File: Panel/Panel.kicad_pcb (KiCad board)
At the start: 2 copper layers, 100 x 100 mm, 83 parts, among them J1 Conn_01x03, J10 Conn_01x02, J11 Conn_01x03, J12 Conn_01x03, J2 USB_C_Receptacle_USB2.0, J3 Conn_01x02, J4 Conn_02x06_Odd_Even, J5 Conn_01x07, J6 Conn_01x02, J7 Conn_01x02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

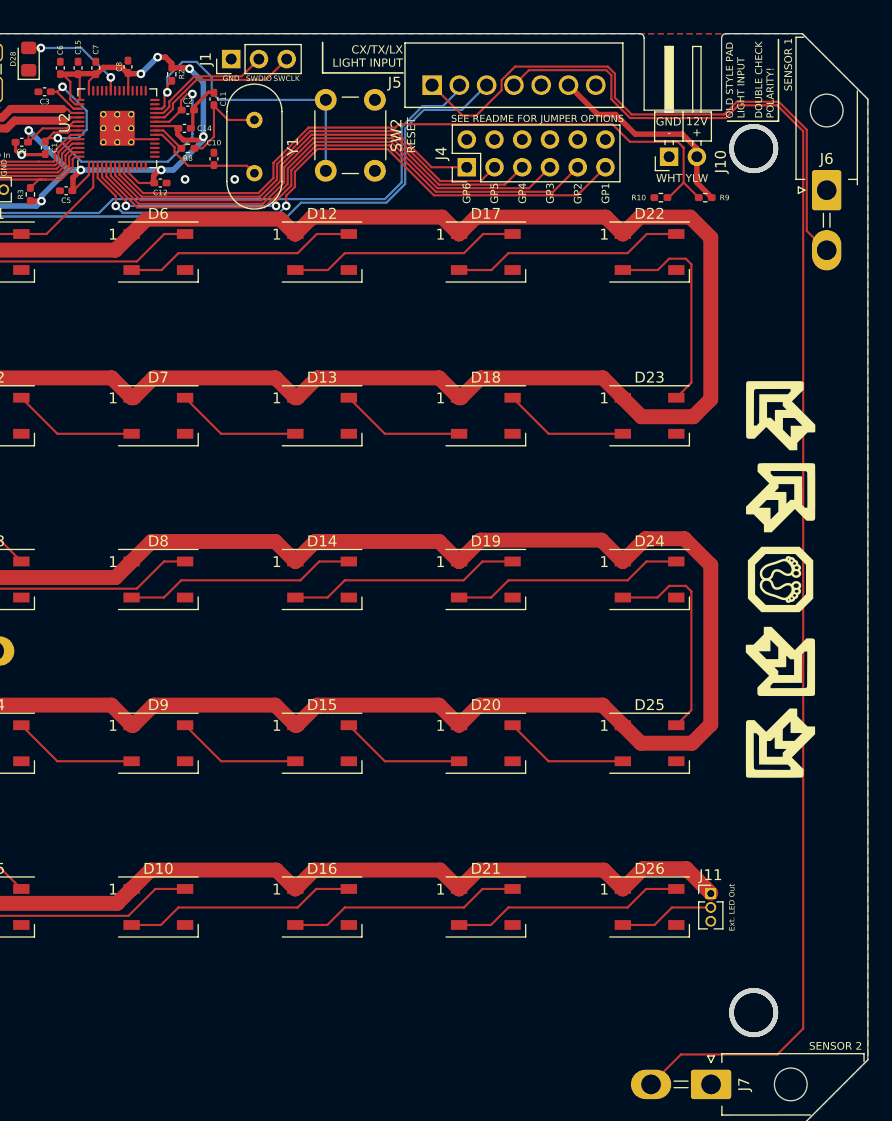
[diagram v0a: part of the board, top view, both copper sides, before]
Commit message: Add RS485 functionality & addons, several fixes
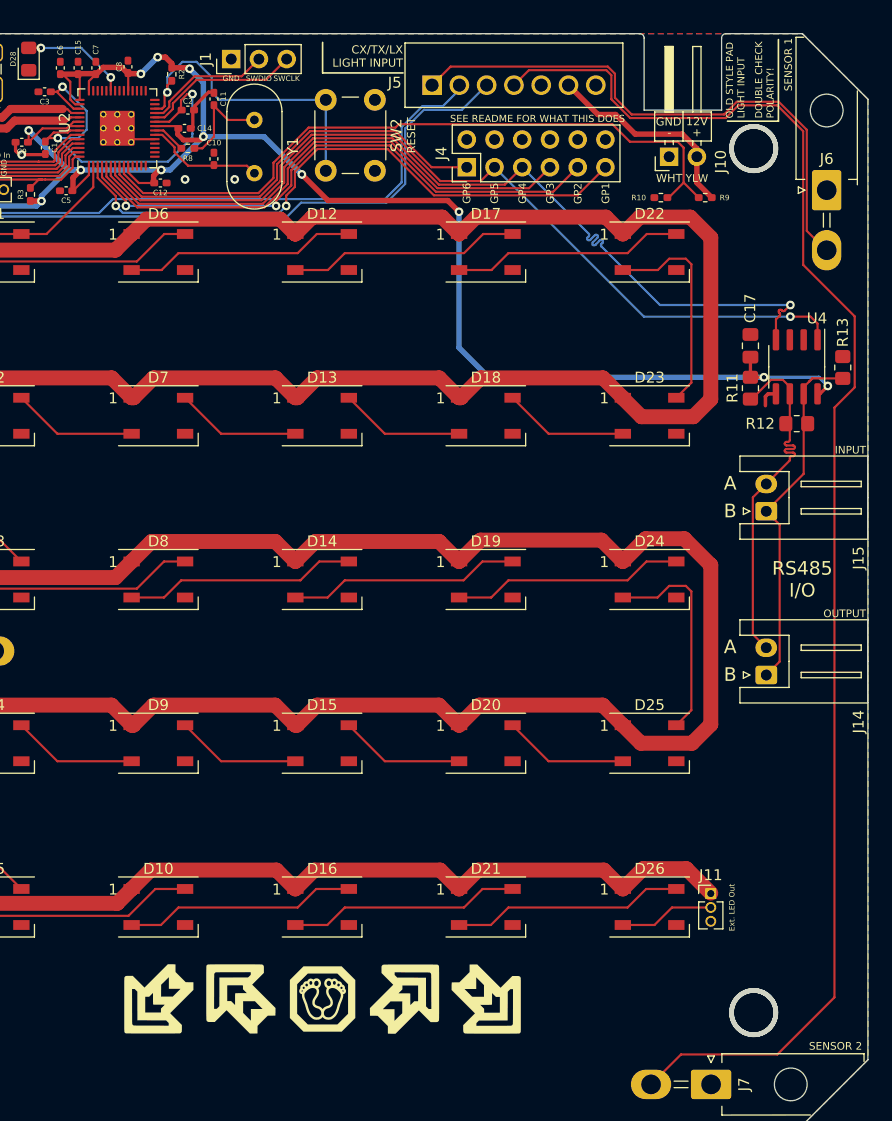
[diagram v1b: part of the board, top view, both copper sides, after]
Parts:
- added C17: 100nF, Capacitor_SMD:C_0805_2012Metric_Pad1.18x1.45mm_HandSolder, F.Cu at (169.2, 78.6)
- added J14: Conn_01x02, Connector_JST:JST_XH_S2B-XH-A_1x02_P2.50mm_Horizontal, F.Cu at (170.7, 108.8)
- added J15: Conn_01x02, Connector_JST:JST_XH_S2B-XH-A_1x02_P2.50mm_Horizontal, F.Cu at (170.7, 93.8)
- added R11: 4.7k, Resistor_SMD:R_0805_2012Metric_Pad1.20x1.40mm_HandSolder, F.Cu at (169.2, 82.5)
- added R12: 120, Resistor_SMD:R_0805_2012Metric_Pad1.20x1.40mm_HandSolder, F.Cu at (173.5, 85.7)
- added R13: 4.7k, Resistor_SMD:R_0805_2012Metric_Pad1.20x1.40mm_HandSolder, F.Cu at (177.7, 80.6)
- added U4: SP3485EN, Package_SO:SOIC-8_3.9x4.9mm_P1.27mm, F.Cu at (173.5, 80.5)
- moved G*** 78.1 mm to (115.0, 138.4), turned to 180 degrees
- moved G*** 67.5 mm to (122.5, 138.4), turned to 90 degrees
- moved G*** 56.9 mm to (130.0, 138.4), turned to 0 degrees
- moved G*** 46.3 mm to (137.5, 138.4), turned to 0 degrees
- moved G*** 35.7 mm to (145.0, 138.4), turned to -90 degrees
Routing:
- net +3V3: track 117.1 -> 195.2 mm, vias 10 -> 14
- net GPIO5: track 42.2 -> 79.2 mm, vias 0 -> 1
- net GPIO4: track 45.4 -> 82.3 mm, vias 0 -> 1
- net /RS485_A: track 0.00 -> 33.4 mm
- net /RS485_B: track 0.00 -> 33.1 mm
- net SENSOR 2: track 129.9 -> 133.8 mm
- net SENSOR 1: track 54.3 -> 51.5 mm
- net GND: track 14.0 -> 15.9 mm
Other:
- board text added: "A"
- board text added: "B"
- board text added: "INPUT"
- board text added: "OUTPUT"
- board text added: "Overkill PIU Pad Lighting Kit Rev. 3"
- board text added: "RS485 I/O"
- board text added: "SEE README FOR WHAT THIS DOES"
- board text removed: "Overkill PIU Pad Lighting Kit Rev. 2"
- board text removed: "SEE README FOR JUMPER OPTIONS"

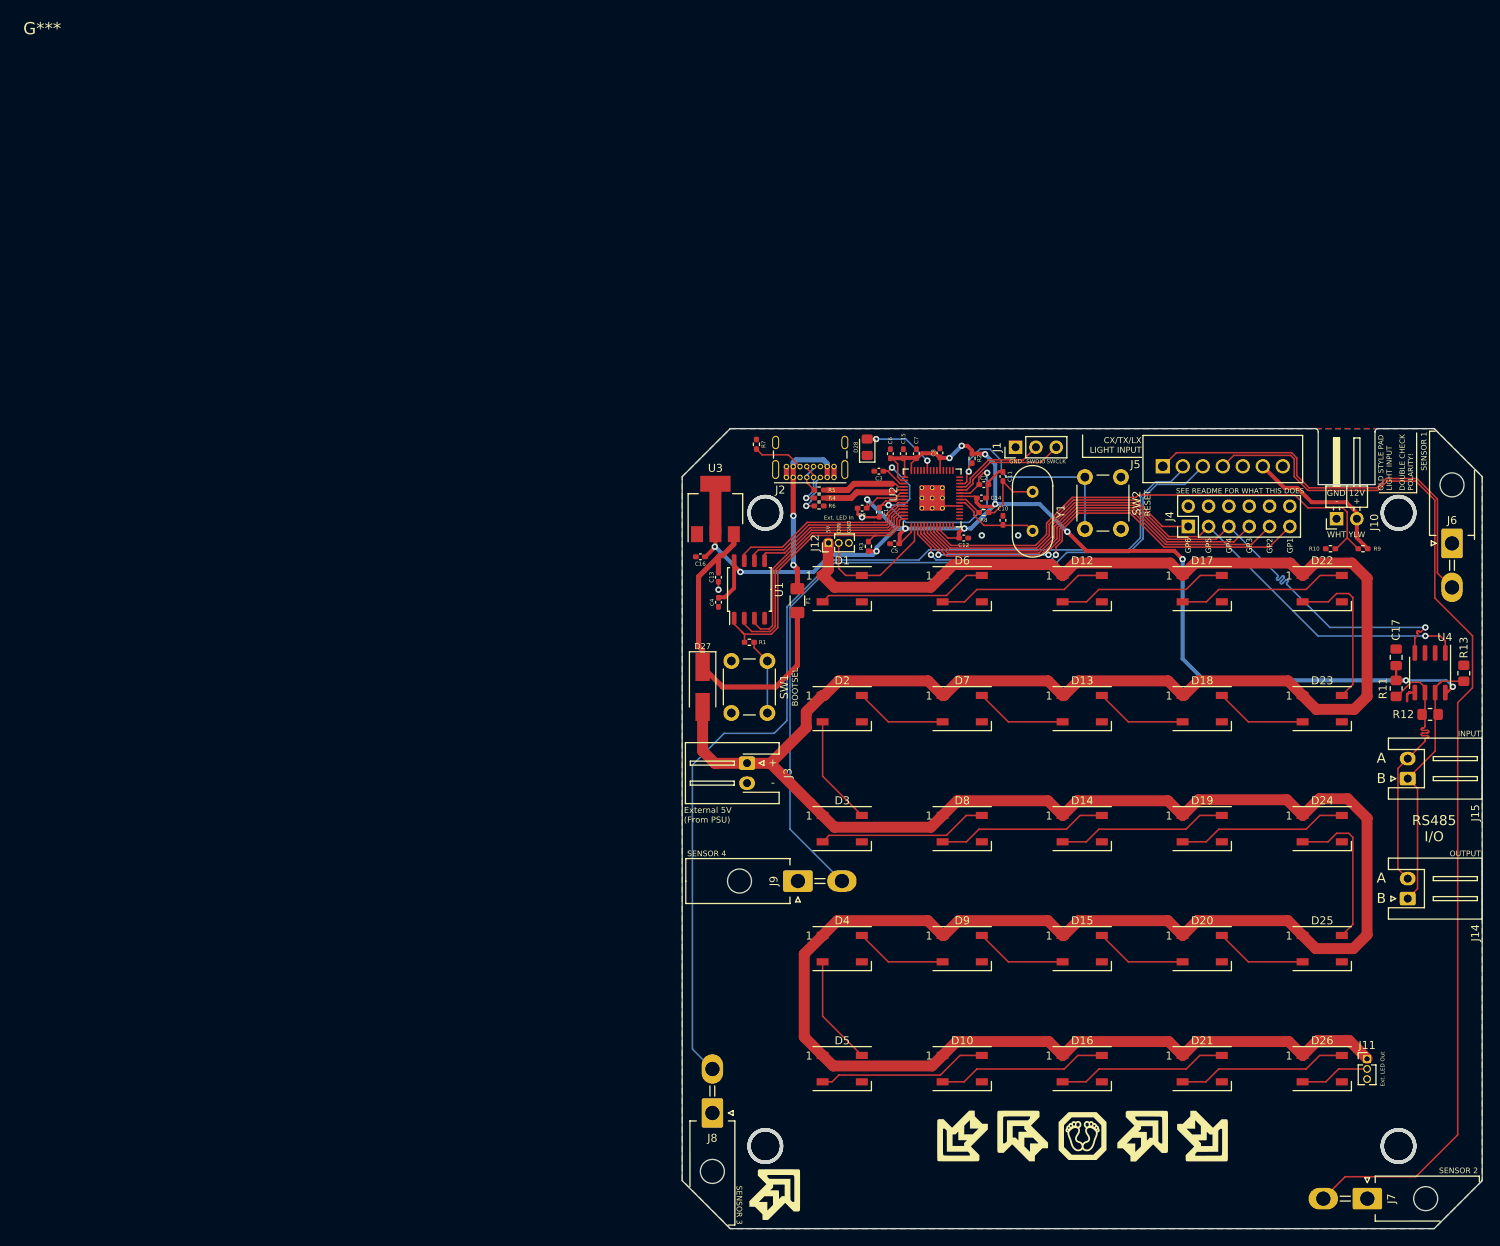
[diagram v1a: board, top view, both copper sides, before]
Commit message: Add voltage divider bypass for home pad use
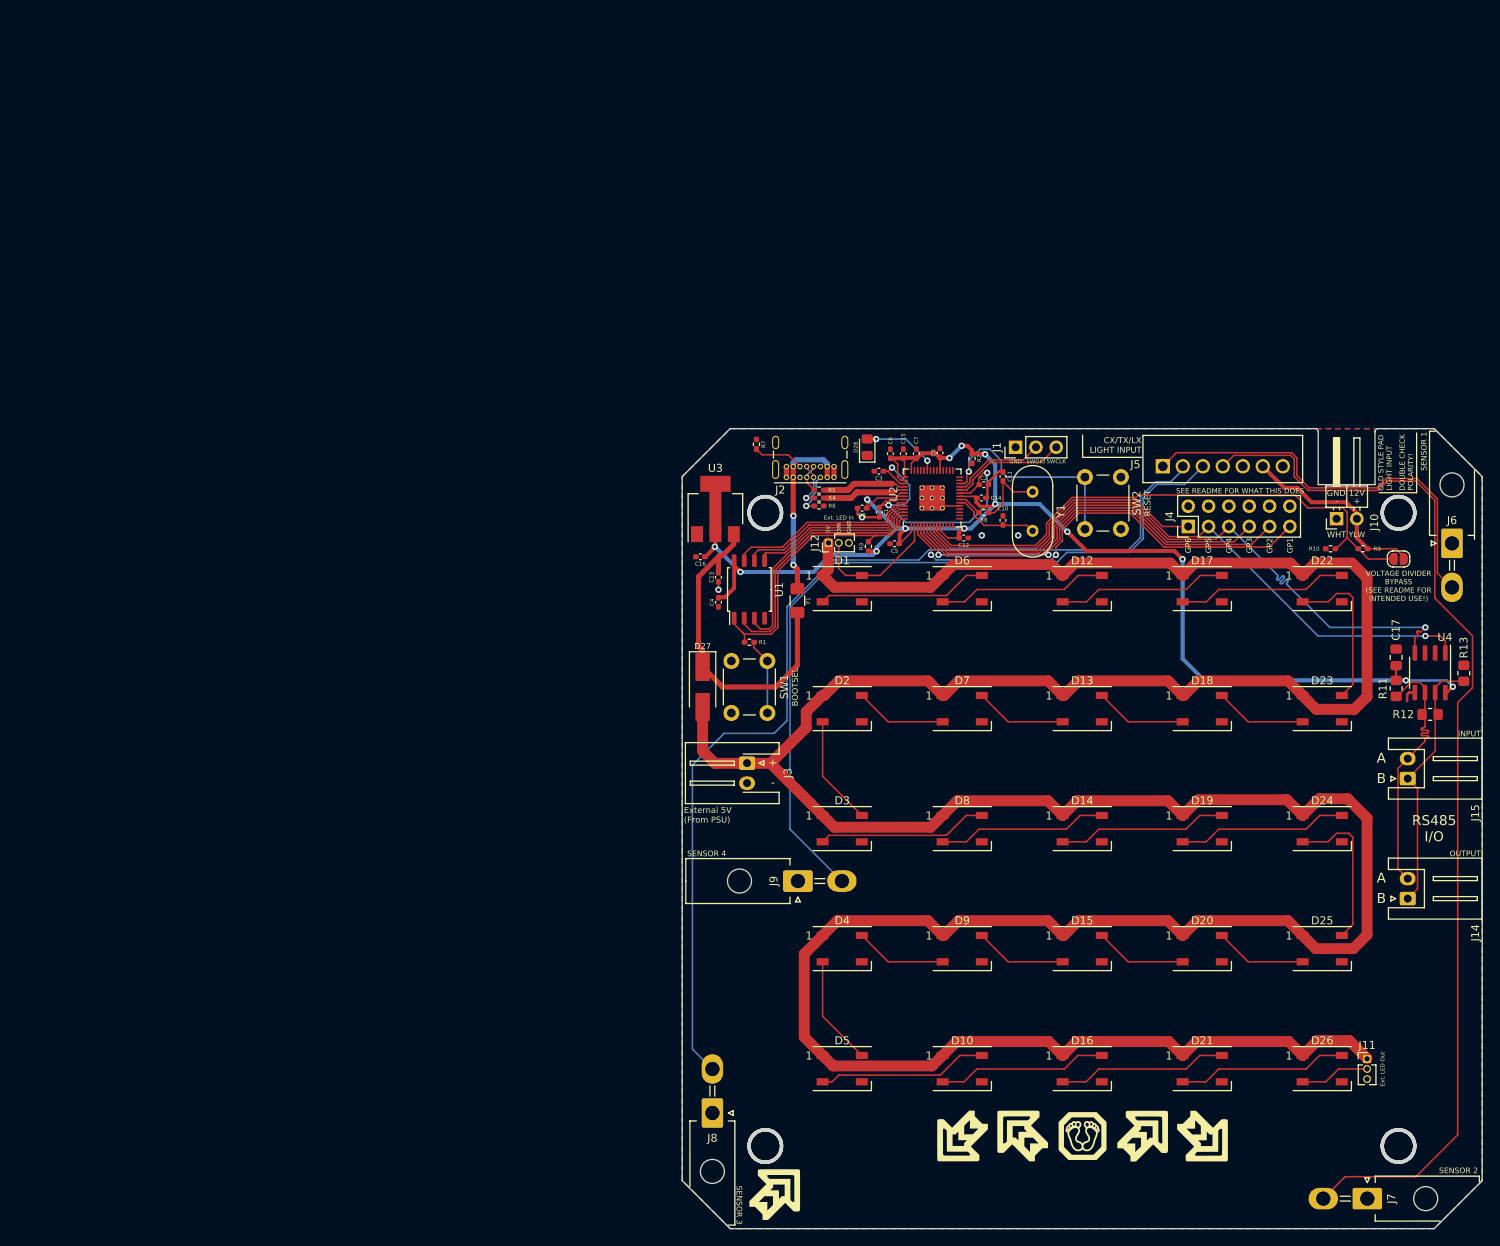
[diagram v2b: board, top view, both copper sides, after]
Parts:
- added JP1: Jumper_2_Open, Jumper:SolderJumper-2_P1.3mm_Open_RoundedPad1.0x1.5mm, F.Cu at (169.5, 66.3)
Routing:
- net LIGHT EN: track 19.2 -> 24.4 mm
- net GPIO7: track 64.3 -> 69.2 mm
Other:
- board text added: "VOLTAGE DIVIDER BYPASS (SEE README FOR INTENDED USE!)"
- board text removed: "G***"
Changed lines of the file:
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@@
     )
   )
+  (footprint "Jumper:SolderJumper-2_P1.3mm_Open_RoundedPad1.0x1.5mm" (layer "F.Cu")
+    (at 169.545 66.294)
+    (descr "SMD Solder Jumper, 1x1.5mm, rounded Pads, 0.3mm gap, open")
+    (tags "solder jumper open")
+    (property "Sheetfile" "Panel.kicad_sch")
+    (property "Sheetname" "")
+    (property "ki_description" "Jumper, 2-pole, open")
+    (property "ki_keywords" "Jumper SPST")
+    (attr exclude_from_pos_files)
+    (fp_text reference "JP1" (at 0 -1.8) (layer "F.SilkS") hide
+        (effects (font (size 1 1) (thickness 0.15)))
+    )
+    (fp_text value "Jumper_2_Open" (at 0 1.9) (layer "F.Fab")
+        (effects (font (size 1 1) (thickness 0.15)))
+    )
+    (fp_line (start -1.4 0.3) (end -1.4 -0.3)
+      (stroke (width 0.12) (type solid)) (layer "F.SilkS"))
+    (fp_line (start -0.7 -1) (end 0.7 -1)
+      (stroke (width 0.12) (type solid)) (layer "F.SilkS"))
+    (fp_line (start 0.7 1) (end -0.7 1)
+      (stroke (width 0.12) (type solid)) (layer "F.SilkS"))
+    (fp_line (start 1.4 -0.3) (end 1.4 0.3)
+      (stroke (width 0.12) (type solid)) (layer "F.SilkS"))
+    (fp_arc (start -1.4 -0.3) (mid -1.194975 -0.794975) (end -0.7 -1)
+      (stroke (width 0.12) (type solid)) (layer "F.SilkS"))
+    (fp_arc (start -0.7 1) (mid -1.194975 0.794975) (end -1.4 0.3)
+      (stroke (width 0.12) (type solid)) (layer "F.SilkS"))
+    (fp_arc (start 0.7 -1) (mid 1.194975 -0.794975) (end 1.4 -0.3)
+      (stroke (width 0.12) (type solid)) (layer "F.SilkS"))
+    (fp_arc (start 1.4 0.3) (mid 1.194975 0.794975) (end 0.7 1)
+      (stroke (width 0.12) (type solid)) (layer "F.SilkS"))
+    (fp_line (start -1.65 -1.25) (end -1.65 1.25)
+      (stroke (width 0.05) (type solid)) (layer "F.CrtYd"))
+    (fp_line (start -1.65 -1.25) (end 1.65 -1.25)
+      (stroke (width 0.05) (type solid)) (layer "F.CrtYd"))
+    (fp_line (start 1.65 1.25) (end -1.65 1.25)
+      (stroke (width 0.05) (type solid)) (layer "F.CrtYd"))
+    (fp_line (start 1.65 1.25) (end 1.65 -1.25)
+      (stroke (width 0.05) (type solid)) (layer "F.CrtYd"))
+    (pad "1" smd custom (at -0.65 0) (size 1 0.5) (layers "F.Cu" "F.Mask")
+      (net 44 "GPIO7") (pinfunction "A") (pintype "passive") (zone_connect 2) (thermal_bridge_angle 45)
+      (options (clearance outline) (anchor rect))
+      (primitives
+        (gr_circle (center 0 0.25) (end 0.5 0.25) (width 0) (fill yes))
+        (gr_circle (center 0 -0.25) (end 0.5 -0.25) (width 0) (fill yes))
+        (gr_poly
+          (pts
+            (xy 0.5 0.75)
+            (xy 0 0.75)
+            (xy 0 -0.75)
+            (xy 0.5 -0.75)
+          )
+          (width 0) (fill yes))
+      ))
+    (pad "2" smd custom (at 0.65 0) (size 1 0.5) (layers "F.Cu" "F.Mask")
+      (net 61 "LIGHT EN") (pinfunction "B") (pintype "passive") (zone_connect 2) (thermal_bridge_angle 45)
+      (options (clearance outline) (anchor rect))
+      (primitives
+        (gr_circle (center 0 0.25) (end 0.5 0.25) (width 0) (fill yes))
+        (gr_circle (center 0 -0.25) (end 0.5 -0.25) (width 0) (fill yes))
+        (gr_poly
+          (pts
+            (xy 0 0.75)
+            (xy -0.5 0.75)
+            (xy -0.5 -0.75)
+            (xy 0 -0.75)
+          )
+          (width 0) (fill yes))
+      ))
+  )
   (footprint "Package_TO_SOT_SMD:SOT-223-3_TabPin2" (layer "F.Cu")
     (at 84.1502 60.0456 90)
@@
     (effects (font (size 0.7 0.7) (thickness 0.125)))
   )
-  (gr_text "G***" (at 0 0) (layer "F.SilkS")
-    (effects (font (size 1.524 1.524) (thickness 0.3)))
+  (gr_text "VOLTAGE DIVIDER\nBYPASS\n(SEE README FOR\nINTENDED USE!)" (at 169.545 71.628) (layer "F.SilkS")
+    (effects (font (size 0.65 0.65) (thickness 0.15)) (justify bottom))
   )
   (gr_text "GND" (at 100.8634 62.280359 90) (layer "F.SilkS")
@@
   (segment (start 140.030792 62.235) (end 136.723792 58.928) (width 0.2) (layer "F.Cu") (net 43))
   (segment (start 125.546 61.824552) (end 128.769552 58.601) (width 0.2) (layer "F.Cu") (net 44))
+  (segment (start 165.780874 66.294) (end 164.5025 65.015626) (width 0.2) (layer "F.Cu") (net 44))
   (segment (start 161.755574 65.015626) (end 163.1188 63.6524) (width 0.2) (layer "F.Cu") (net 44))
   (segment (start 113.607688 64.605) (end 124.161242 64.605) (width 0.2) (layer "F.Cu") (net 44))
   (segment (start 128.769552 58.601) (end 136.725 58.601) (width 0.2) (layer "F.Cu") (net 44))
+  (segment (start 168.895 66.294) (end 165.780874 66.294) (width 0.2) (layer "F.Cu") (net 44))
   (segment (start 136.725 58.601) (end 137.033 58.293) (width 0.2) (layer "F.Cu") (net 44))
   (segment (start 163.1188 60.4428) (end 163.1188 63.631926) (width 0.2) (layer "F.Cu") (net 44))
@@
   (segment (start 171.704 143.51) (end 162.8782 143.51) (width 0.2) (layer "F.Cu") (net 60))
   (segment (start 152.574 54.712) (end 155.266 57.404) (width 0.5) (layer "F.Cu") (net 61))
+  (segment (start 169.187654 65.015626) (end 165.6975 65.015626) (width 0.2) (layer "F.Cu") (net 61))
   (segment (start 164.333 61.271) (end 164.333 63.651126) (width 0.5) (layer "F.Cu") (net 61))
   (segment (start 164.333 60.533) (end 164.333 61.271) (width 0.5) (layer "F.Cu") (net 61))
   (segment (start 156.8875 57.404) (end 158.6835 59.2) (width 0.5) (layer "F.Cu") (net 61))
   (segment (start 163 59.2) (end 164.333 60.533) (width 0.5) (layer "F.Cu") (net 61))
+  (segment (start 170.195 66.022972) (end 169.187654 65.015626) (width 0.2) (layer "F.Cu") (net 61))
   (segment (start 155.266 57.404) (end 156.8875 57.404) (width 0.5) (layer "F.Cu") (net 61))
+  (segment (start 170.195 66.294) (end 170.195 66.022972) (width 0.2) (layer "F.Cu") (net 61))
   (segment (start 164.333 63.651126) (end 165.6975 65.015626) (width 0.5) (layer "F.Cu") (net 61))
   (segment (start 158.6835 59.2) (end 163 59.2) (width 0.5) (layer "F.Cu") (net 61))
